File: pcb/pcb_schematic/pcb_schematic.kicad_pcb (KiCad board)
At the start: 4 copper layers, 41.5 x 48.3 mm, 37 parts, among them J1 Conn_ST_STDC14, J3 Conn_02x02_Odd_Even, J4 USB_B_Micro, Q1 MMBT3904, Q2 MMBT3904, Q3 MMBT3904, U1 STM32G031K8Tx, U2 NCP1117-3.3_SOT223, U4 SSD1306 128 x 64 OLED (0x3C), U5 TCS34725 (0x29), Y1 Crystal

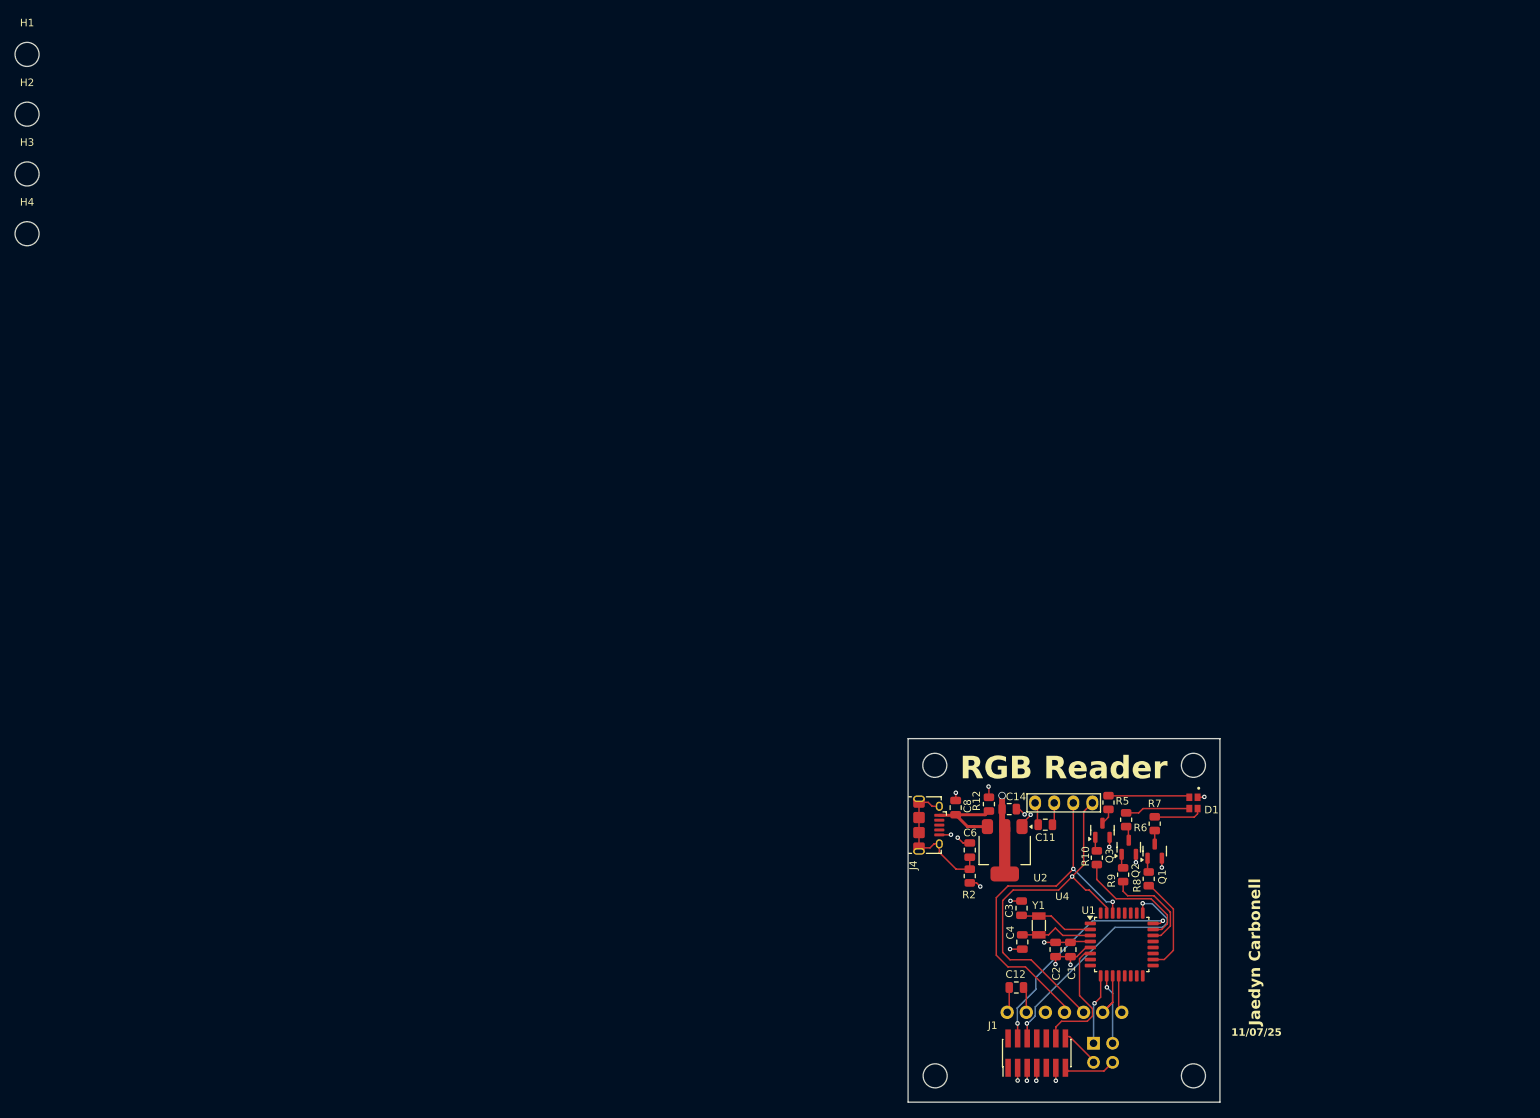
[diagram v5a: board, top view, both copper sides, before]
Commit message: via warning
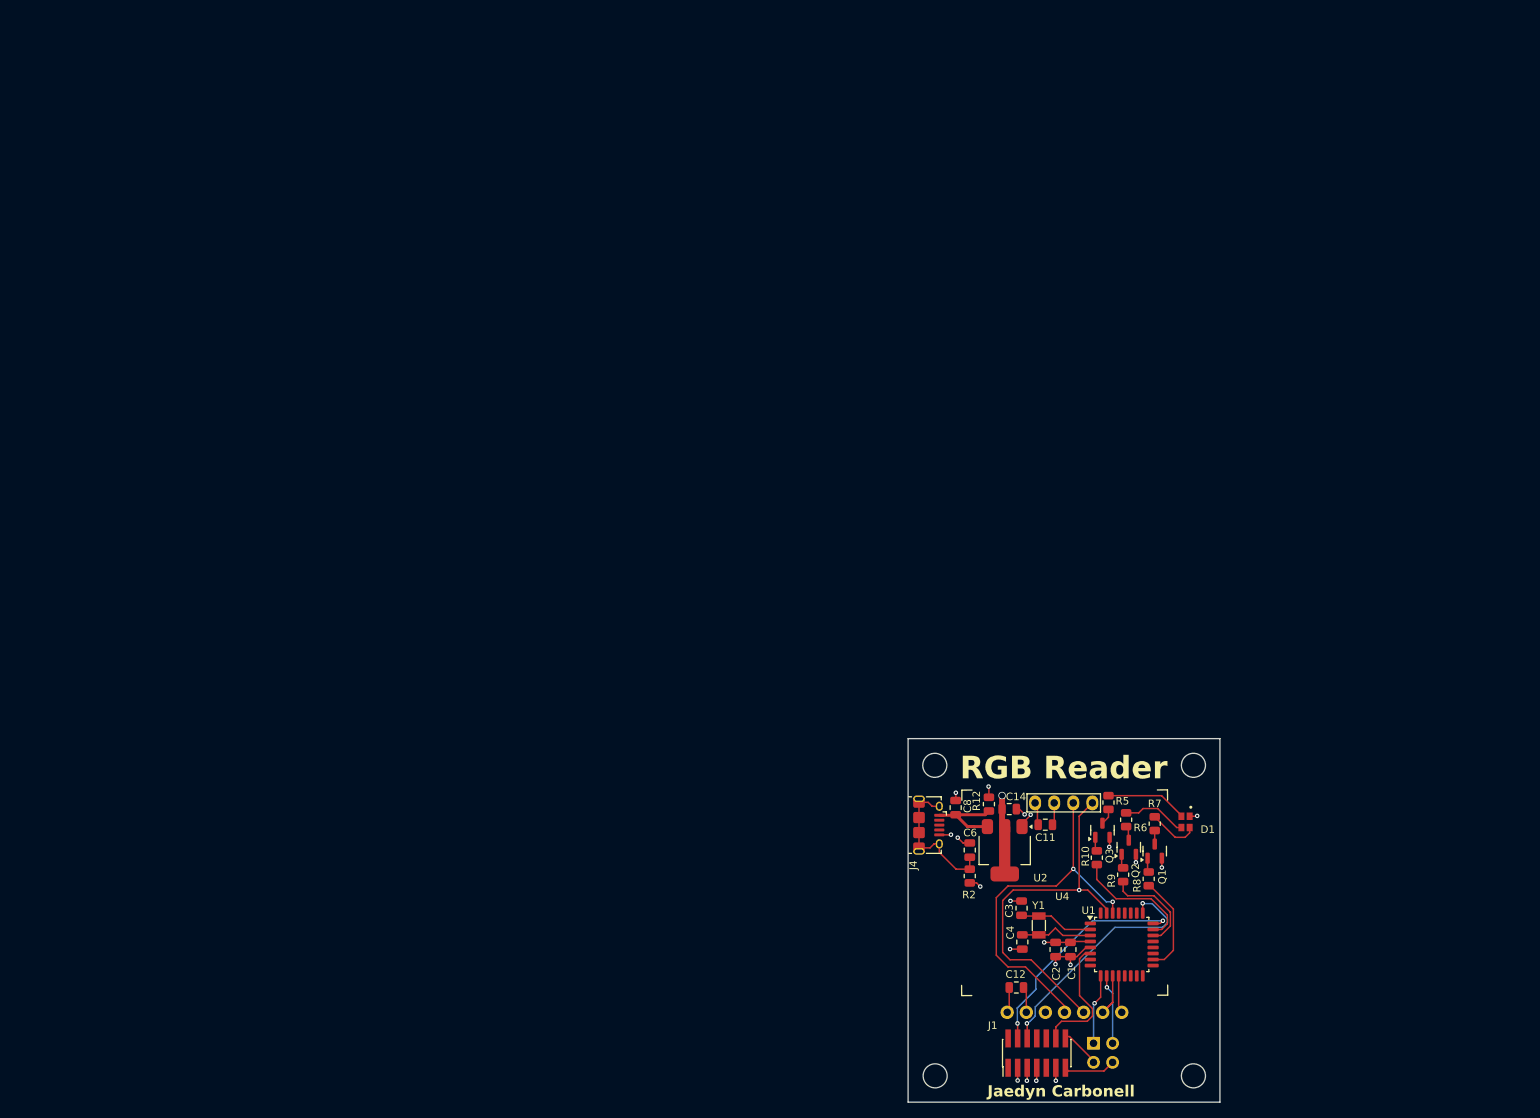
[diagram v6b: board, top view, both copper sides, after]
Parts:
- removed the H1 at (3.48, 3.48)
- removed the H2 at (3.48, 11.4)
- removed the H3 at (3.48, 19.4)
- removed the H4 at (3.48, 27.3)
- moved D1 2.73 mm to (157.6, 105.5)
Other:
- board text added: "Created Nov. 7, 2025"
- board text added: "TCS34725"
- board text removed: "11/07/25"

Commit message: added image lol
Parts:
- added G***: LOGO, LOGO, F.Cu at (186.9, 111.0)

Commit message: Finalized?
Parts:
- removed the G*** at (186.9, 111.0)
- added G***: LOGO, LOGO, F.Cu at (170.9, 116.4)
- added G***: LOGO, LOGO, B.Cu at (153.8, 94.2)
- moved D1 22.2 mm to (171.3, 88.2)
- moved J1 19.6 mm to (150.4, 121.3)
- moved J3 19.6 mm to (158.0, 120.0)
- moved C11 19.6 mm to (151.5, 90.9)
- moved C12 19.6 mm to (147.7, 112.6)
- moved C14 19.6 mm to (146.7, 88.8)
- moved C6 19.6 mm to (141.5, 94.3)
- moved C8 19.6 mm to (139.6, 88.6)
- moved H2 19.6 mm to (171.2, 83.0)
- moved J4 19.6 mm to (136.0, 91.0)
- moved Q1 19.6 mm to (166.1, 94.4)
- moved Q2 19.6 mm to (162.6, 93.9)
- moved Q3 19.6 mm to (159.1, 91.7)
- moved R10 19.6 mm to (158.4, 95.3)
- moved R12 19.6 mm to (144.0, 88.2)
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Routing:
- added copper zone on B.Cu, net GND
- added copper zone on F.Cu, net GND
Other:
- board size 41.5 x 48.3 mm -> 41.5 x 48.4 mm
- board text added: "Created: Nov 2025"
- board text removed: "Created Nov. 7, 2025"
